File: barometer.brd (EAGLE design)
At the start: 58.4 x 38.4 mm, 90 parts, among them IC1 MIC5225-3.3v, IC2 TPS5410, IC3 ZPA2326-0311A-R, U1 MCP4725, U2 LTC2850, U3 PCA9306, U4 MAX3221, U5 XC6215XC6215B182NR, U6 Tiny85-20-SMT, X2 1751264, X3 1751248

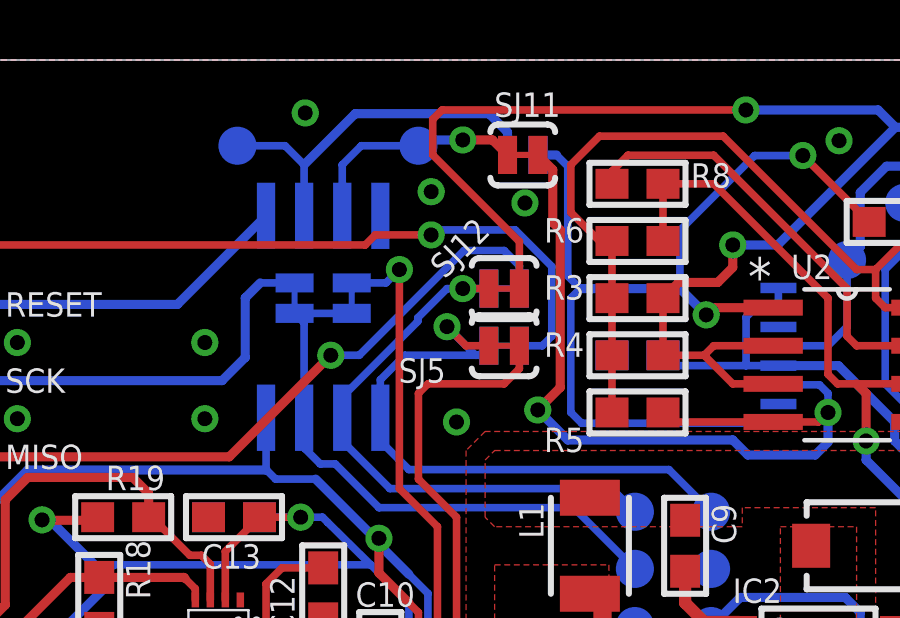
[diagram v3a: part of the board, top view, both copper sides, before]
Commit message: Beautify vias and silkscreen text
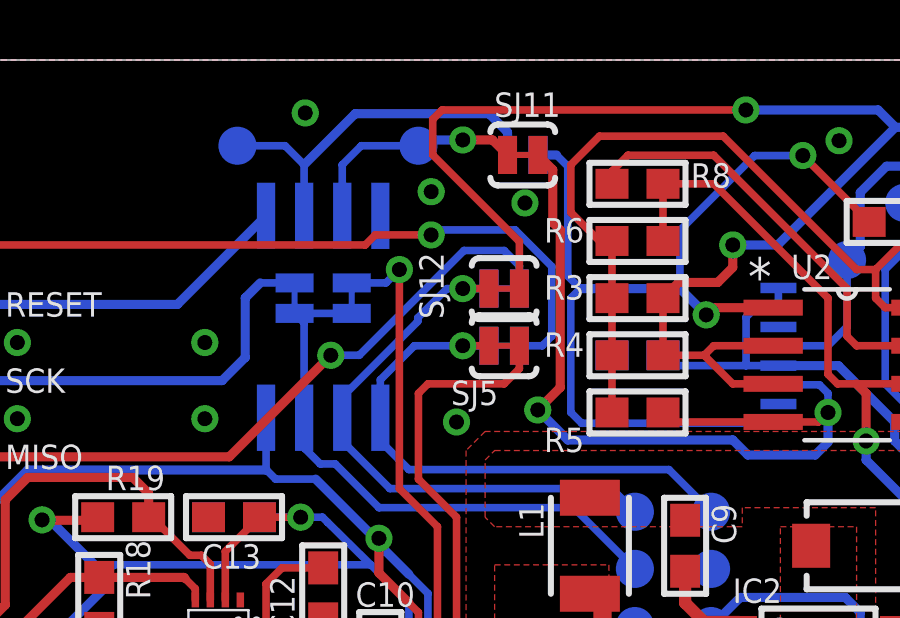
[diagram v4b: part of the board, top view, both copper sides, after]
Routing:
- net B0: track 21.3 -> 19.2 mm
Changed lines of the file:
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@@
 </element>
 <element name="SJ5" library="SparkFun-Retired" package="SJ_2S-TRACE" value="SOLDERJUMPERTRACE" x="24.13" y="28.89" smashed="yes">
-<attribute name="NAME" x="20.61" y="27.66" size="0.8128" layer="25" font="vector" ratio="18"/>
+<attribute name="NAME" x="22.36" y="26.91" size="0.8128" layer="25" font="vector" ratio="18"/>
 </element>
 <element name="SJ6" library="SparkFun-Retired" package="SJ_2S-TRACE" value="SOLDERJUMPERTRACE" x="19.05" y="30.4775" smashed="yes" rot="MR90">
@@
 </element>
 <element name="SJ12" library="SparkFun-Retired" package="SJ_2S-TRACE" value="SOLDERJUMPERTRACE" x="24.13" y="30.795" smashed="yes">
-<attribute name="NAME" x="22.14944375" y="31.092728125" size="0.8128" layer="25" font="vector" ratio="18" rot="R45"/>
+<attribute name="NAME" x="22.113325" y="31.9944625" size="0.8128" layer="25" font="vector" ratio="18" rot="R90" align="bottom-right"/>
 </element>
 </elements>
@@
 <contactref element="TP13" pad="TP"/>
 <wire x1="20.0025" y1="26.4897" x2="20.0025" y2="27.755" width="0.254" layer="16"/>
-<wire x1="20.0025" y1="27.755" x2="20.82" y2="28.5725" width="0.254" layer="16"/>
-<wire x1="20.82" y1="28.5725" x2="23.1775" y2="28.5725" width="0.254" layer="16"/>
-<wire x1="23.1775" y1="28.5725" x2="23.3045" y2="28.5725" width="0.254" layer="16"/>
-<wire x1="23.3045" y1="28.5725" x2="23.622" y2="28.89" width="0.254" layer="16"/>
-<via x="22.225" y="29.525" extent="1-16" drill="0.5"/>
-<wire x1="22.225" y1="29.525" x2="23.1775" y2="28.5725" width="0.254" layer="16"/>
-<wire x1="23.622" y1="28.89" x2="22.86" y2="28.89" width="0.254" layer="1"/>
-<wire x1="22.86" y1="28.89" x2="22.225" y2="29.525" width="0.254" layer="1"/>
+<wire x1="20.0025" y1="27.755" x2="21.1375" y2="28.89" width="0.254" layer="16"/>
+<via x="22.75" y="28.89" extent="1-16" drill="0.5"/>
 <wire x1="20.1422" y1="26.35" x2="20.0025" y2="26.4897" width="0.254" layer="16"/>
 <wire x1="29.6225" y1="24.7625" x2="20.955" y2="24.7625" width="0.254" layer="16"/>
@@
 <wire x1="20.0025" y1="25.715" x2="20.0025" y2="26.4897" width="0.254" layer="16"/>
 <wire x1="31.0275" y1="23.3575" x2="29.6225" y2="24.7625" width="0.254" layer="16"/>
+<wire x1="21.1375" y1="28.89" x2="22.75" y2="28.89" width="0.254" layer="16"/>
+<wire x1="23.622" y1="28.89" x2="22.75" y2="28.89" width="0.254" layer="1"/>
+<wire x1="23.622" y1="28.89" x2="22.75" y2="28.89" width="0.254" layer="16"/>
 </signal>
 <signal name="B2">
